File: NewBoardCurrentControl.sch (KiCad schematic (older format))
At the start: 19 parts, among them Q1 RSR030N06TL, U6 ADA4528-2ACPZ-RL, U7 782853152_WE-CBA_08

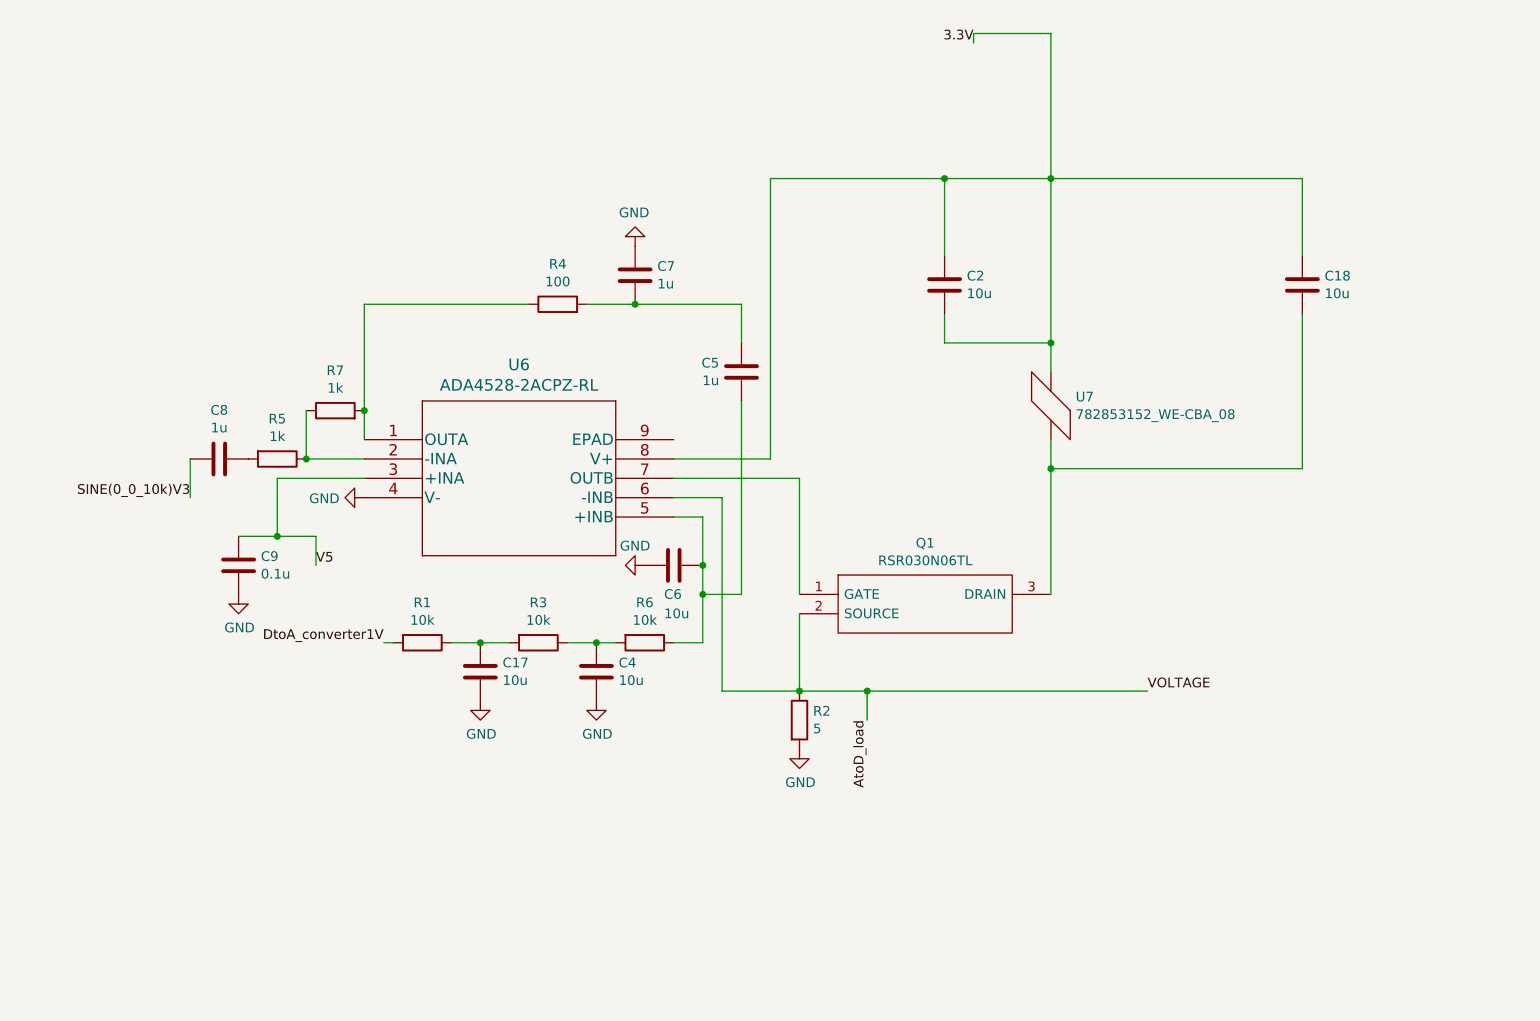
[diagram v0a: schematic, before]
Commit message: QA'd, added 2 caps, noted where laser should be
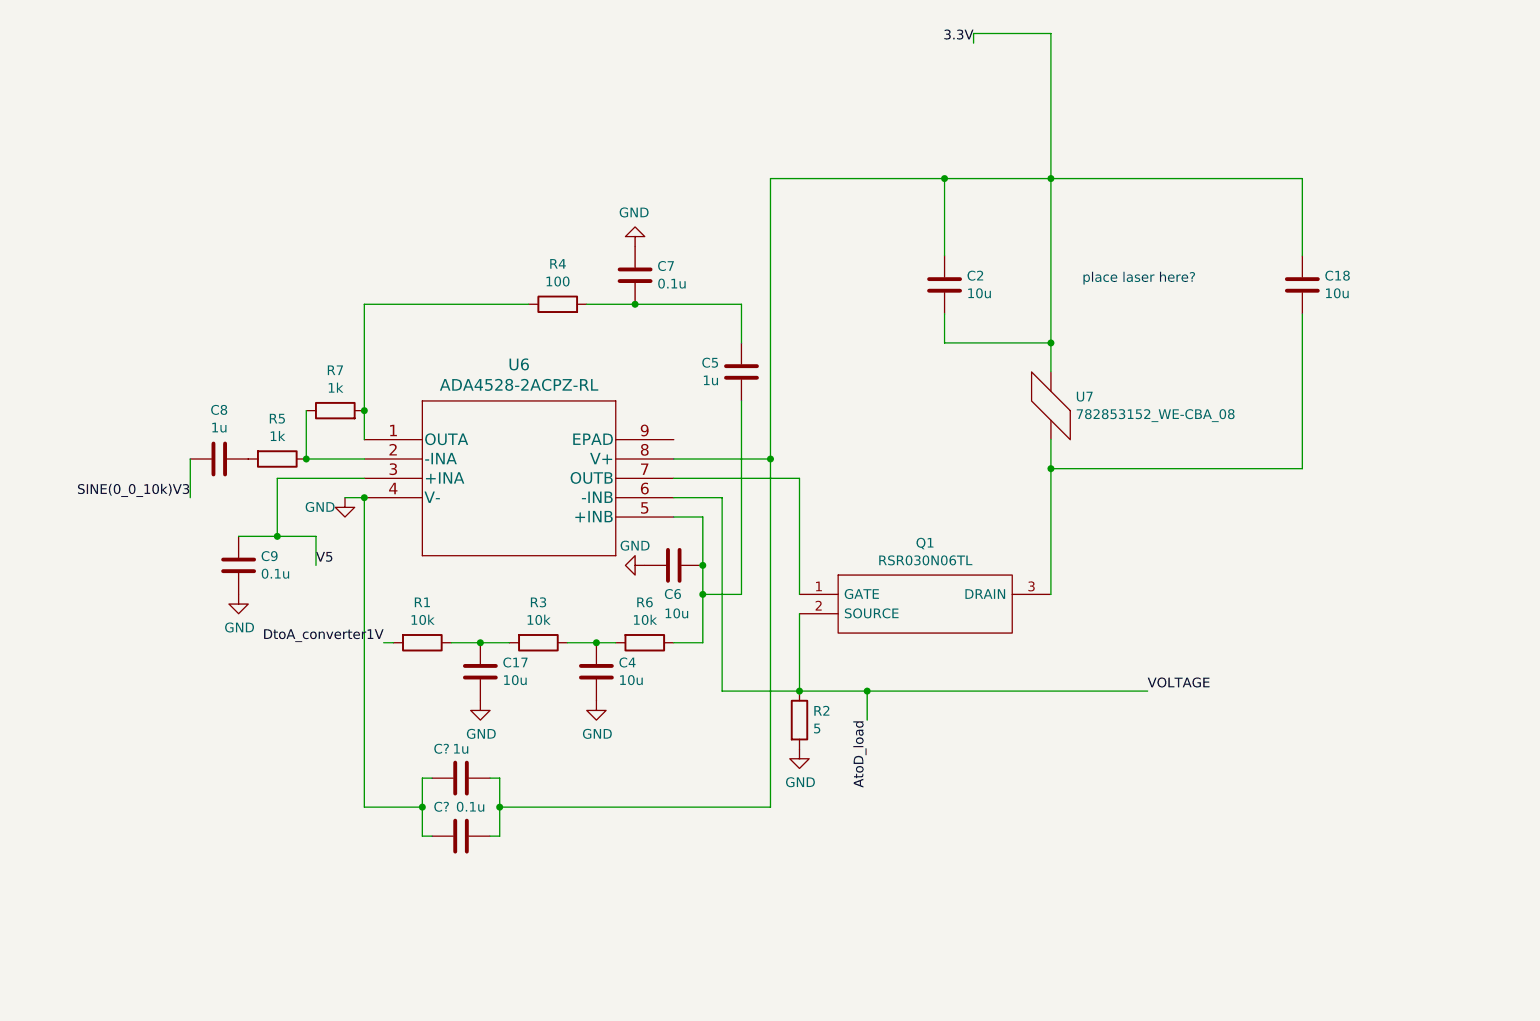
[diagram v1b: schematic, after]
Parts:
- added C?: 1u, symbol Device:C
- added C?: 0.1u, symbol Device:C
- C7: value 1u -> 0.1u
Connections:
- net 3.3V: now also C?.1, C?.1
- net GND: now also C?.2, C?.2
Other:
- note added: "place laser here?\n"
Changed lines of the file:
@@
 L power:GND #PWR0102
 U 1 1 60C997A8
-P 4500 3850
-F 0 "#PWR0102" H 4500 3600 50  0001 C CNN
-F 1 "GND" V 4505 3722 50  0000 R CNN
-F 2 "" H 4500 3850 50  0001 C CNN
-F 3 "" H 4500 3850 50  0001 C CNN
-	1    4500 3850
-	0    1    1    0
+P 4400 3850
+F 0 "#PWR0102" H 4400 3600 50  0001 C CNN
+F 1 "GND" H 4350 3800 50  0000 R CNN
+F 2 "" H 4400 3850 50  0001 C CNN
+F 3 "" H 4400 3850 50  0001 C CNN
+	1    4400 3850
+	1    0    0    -1
 $EndComp
 $Comp
@@
 P 5900 2700
 F 0 "C7" H 6015 2746 50  0000 L CNN
-F 1 "1u" H 6015 2655 50  0000 L CNN
+F 1 "0.1u" H 6015 2655 50  0000 L CNN
 F 2 "" H 5938 2550 50  0001 C CNN
 F 3 "~" H 5900 2700 50  0001 C CNN
@@
 Wire Wire Line
 	8050 3550 8050 3700
+Wire Wire Line
+	4500 3850 4500 5450
+Wire Wire Line
+	4500 5450 4800 5450
+Wire Wire Line
+	4800 5450 4800 5300
+Wire Wire Line
+	4800 5300 4850 5300
+$Comp
+L Device:C C?
+U 1 1 60D13632
+P 5000 5300
+F 0 "C?" V 4850 5200 50  0000 C CNN
+F 1 "1u" V 4850 5300 50  0000 C CNN
+F 2 "" H 5038 5150 50  0001 C CNN
+F 3 "~" H 5000 5300 50  0001 C CNN
+	1    5000 5300
+	0    1    1    0
+$EndComp
+$Comp
+L Device:C C?
+U 1 1 60D13F2E
+P 5000 5600
+F 0 "C?" V 4850 5500 50  0000 C CNN
+F 1 "0.1u" V 4850 5650 50  0000 C CNN
+F 2 "" H 5038 5450 50  0001 C CNN
+F 3 "~" H 5000 5600 50  0001 C CNN
+	1    5000 5600
+	0    1    1    0
+$EndComp
+Wire Wire Line
+	4800 5450 4800 5600
+Wire Wire Line
+	4800 5600 4850 5600
+Connection ~ 4800 5450
+Wire Wire Line
+	5150 5600 5200 5600
+Wire Wire Line
+	5200 5600 5200 5450
+Wire Wire Line
+	5200 5450 6600 5450
+Wire Wire Line
+	6600 5450 6600 3650
+Connection ~ 6600 3650
+Wire Wire Line
+	5150 5300 5200 5300
+Wire Wire Line
+	5200 5300 5200 5450
+Connection ~ 5200 5450
+Wire Wire Line
+	4500 3850 4400 3850
+Connection ~ 4500 3850
+Text Notes 8800 2750 2    50   ~ 0
+place laser here?\n
 $EndSCHEMATC

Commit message: cache
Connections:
- net 3.3V renamed V2_3.3V
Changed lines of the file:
@@
 Wire Wire Line
 	8050 1450 7650 1450
-Wire Wire Line
-	7650 1450 7650 1500
 $Comp
 L Device:C C2
@@
 Text Label 4250 4200 0    50   ~ 0
 V5
-Text Label 7650 1500 2    50   ~ 0
-3.3V
 Connection ~ 8050 3050
 Connection ~ 8050 3700
@@
 Text Notes 8800 2750 2    50   ~ 0
 place laser here?\n
+Text Label 7650 1450 2    50   ~ 0
+V2_3.3V
 $EndSCHEMATC

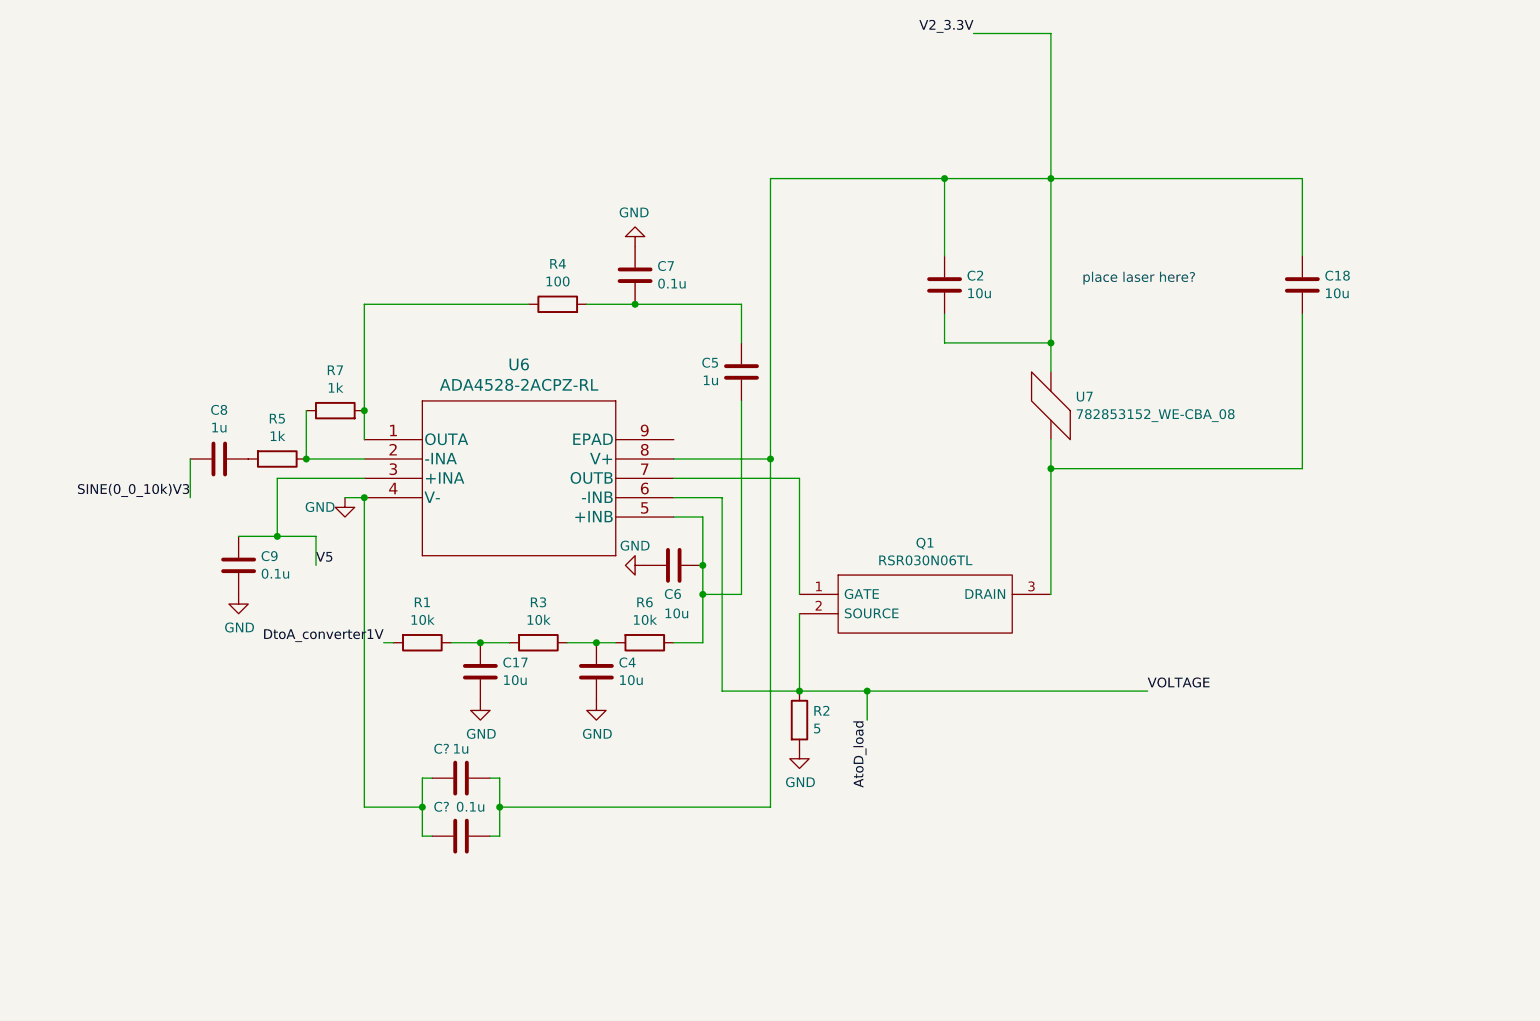
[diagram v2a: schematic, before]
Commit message: annotate all sheets
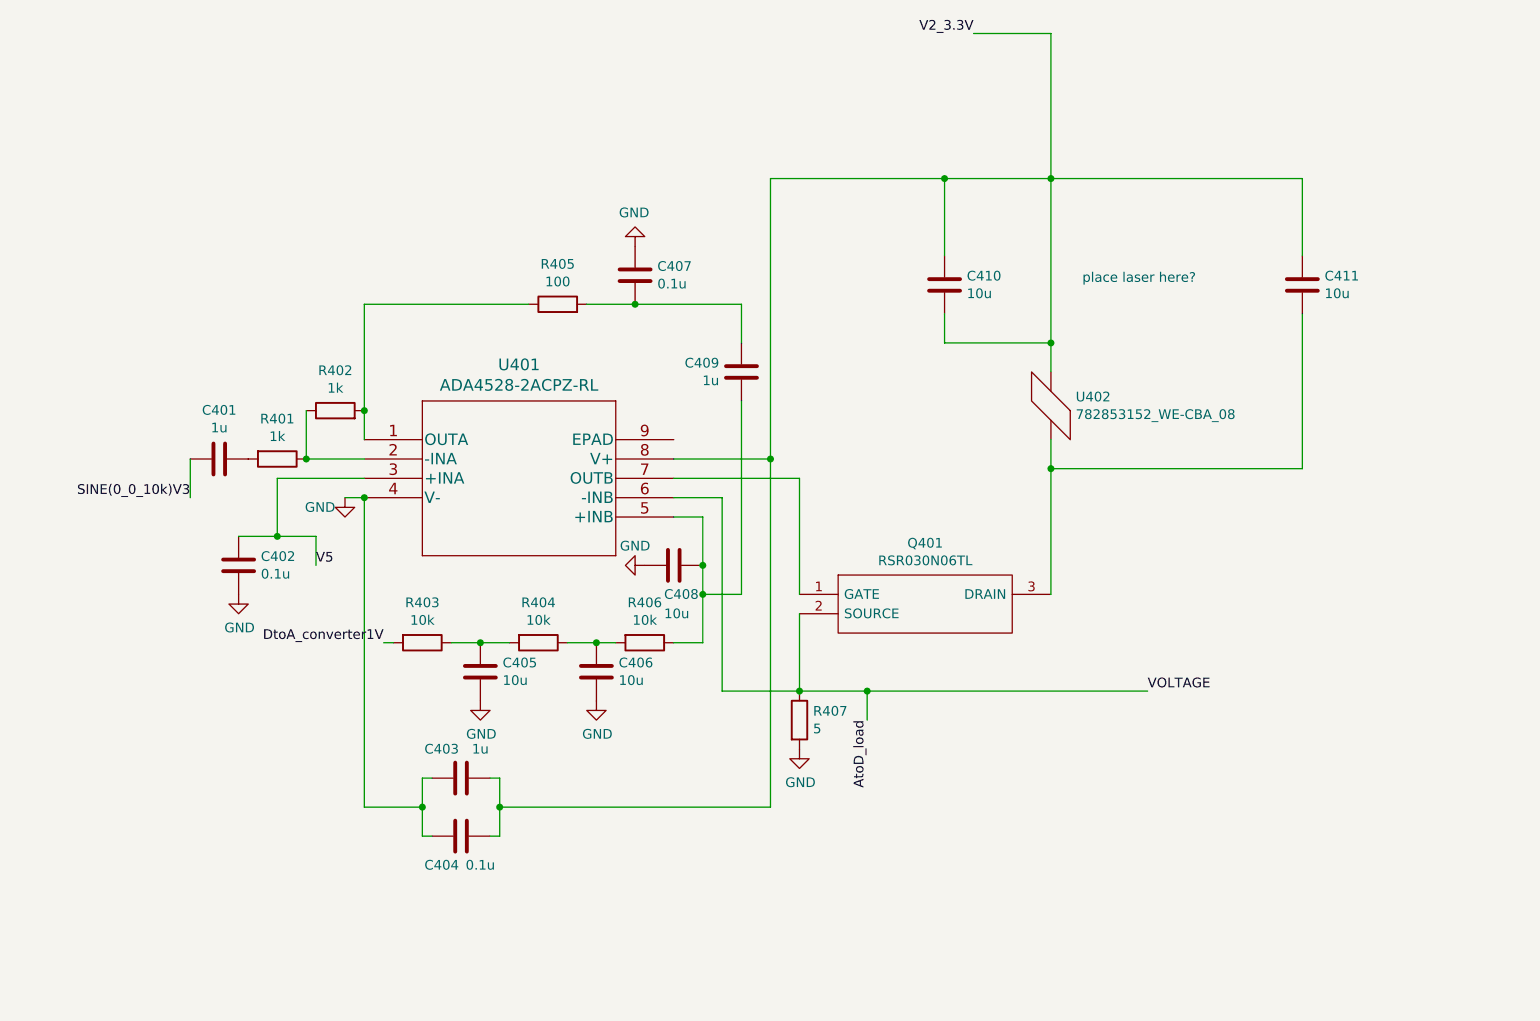
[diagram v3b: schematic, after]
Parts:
- gave numbers to parts that had none: 2
- renumbered C8 to C401, C9 to C402, C17 to C405, C4 to C406, C7 to C407, C6 to C408, C5 to C409, C2 to C410, C18 to C411, Q1 to Q401, R5 to R401, R7 to R402, R1 to R403, R3 to R404, R4 to R405, R6 to R406, R2 to R407, U6 to U401, U7 to U402
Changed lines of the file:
@@
 $EndDescr
 $Comp
-L ADA4528-2ACPZ-RL:ADA4528-2ACPZ-RL U6
+L ADA4528-2ACPZ-RL:ADA4528-2ACPZ-RL U401
 U 1 1 60C850F4
 P 4500 3550
-F 0 "U6" H 5300 3937 60  0000 C CNN
+F 0 "U401" H 5300 3937 60  0000 C CNN
 F 1 "ADA4528-2ACPZ-RL" H 5300 3831 60  0000 C CNN
 F 2 "CP_8_11_ADI" H 5300 3790 60  0001 C CNN
@@
 $EndComp
 $Comp
-L RSR030N06TL:RSR030N06TL Q1
+L RSR030N06TL:RSR030N06TL Q401
 U 1 1 60C86B21
 P 6750 4350
-F 0 "Q1" H 7400 4615 50  0000 C CNN
+F 0 "Q401" H 7400 4615 50  0000 C CNN
 F 1 "RSR030N06TL" H 7400 4524 50  0000 C CNN
 F 2 "SOT95P280X100-3N" H 7900 4450 50  0001 L CNN
@@
 	8050 1450 7650 1450
 $Comp
-L Device:C C2
+L Device:C C410
 U 1 1 60C8E619
 P 7500 2750
-F 0 "C2" H 7615 2796 50  0000 L CNN
+F 0 "C410" H 7615 2796 50  0000 L CNN
 F 1 "10u" H 7615 2705 50  0000 L CNN
 F 2 "" H 7538 2600 50  0001 C CNN
@@
 $EndComp
 $Comp
-L Device:C C18
+L Device:C C411
 U 1 1 60C8ED48
 P 9350 2750
-F 0 "C18" H 9465 2796 50  0000 L CNN
+F 0 "C411" H 9465 2796 50  0000 L CNN
 F 1 "10u" H 9465 2705 50  0000 L CNN
 F 2 "" H 9388 2600 50  0001 C CNN
@@
 Connection ~ 6750 4850
 $Comp
-L Device:R R2
+L Device:R R407
 U 1 1 60C96966
 P 6750 5000
-F 0 "R2" H 6820 5046 50  0000 L CNN
+F 0 "R407" H 6820 5046 50  0000 L CNN
 F 1 "5" H 6820 4955 50  0000 L CNN
 F 2 "" V 6680 5000 50  0001 C CNN
@@
 $EndComp
 $Comp
-L power:GND #PWR0101
+L power:GND #PWR0407
 U 1 1 60C97896
 P 6750 5150
-F 0 "#PWR0101" H 6750 4900 50  0001 C CNN
+F 0 "#PWR0407" H 6750 4900 50  0001 C CNN
 F 1 "GND" H 6755 4977 50  0000 C CNN
 F 2 "" H 6750 5150 50  0001 C CNN
@@
 	7100 4850 8550 4850
 $Comp
-L power:GND #PWR0102
+L power:GND #PWR0402
 U 1 1 60C997A8
 P 4400 3850
-F 0 "#PWR0102" H 4400 3600 50  0001 C CNN
+F 0 "#PWR0402" H 4400 3600 50  0001 C CNN
 F 1 "GND" H 4350 3800 50  0000 R CNN
 F 2 "" H 4400 3850 50  0001 C CNN
@@
 $EndComp
 $Comp
-L Device:R R6
+L Device:R R406
 U 1 1 60C9BFE0
 P 5950 4600
-F 0 "R6" V 5743 4600 50  0000 C CNN
+F 0 "R406" V 5743 4600 50  0000 C CNN
 F 1 "10k" V 5834 4600 50  0000 C CNN
 F 2 "" V 5880 4600 50  0001 C CNN
@@
 	5800 4600 5700 4600
 $Comp
-L Device:C C4
+L Device:C C406
 U 1 1 60C9CF21
 P 5700 4750
-F 0 "C4" H 5815 4796 50  0000 L CNN
+F 0 "C406" H 5815 4796 50  0000 L CNN
 F 1 "10u" H 5815 4705 50  0000 L CNN
 F 2 "" H 5738 4600 50  0001 C CNN
@@
 Connection ~ 5700 4600
 $Comp
-L power:GND #PWR0103
+L power:GND #PWR0404
 U 1 1 60C9DA38
 P 5700 4900
-F 0 "#PWR0103" H 5700 4650 50  0001 C CNN
+F 0 "#PWR0404" H 5700 4650 50  0001 C CNN
 F 1 "GND" H 5705 4727 50  0000 C CNN
 F 2 "" H 5700 4900 50  0001 C CNN
@@
 	5700 4600 5550 4600
 $Comp
-L Device:R R3
+L Device:R R404
 U 1 1 60C9E5A0
 P 5400 4600
-F 0 "R3" V 5193 4600 50  0000 C CNN
+F 0 "R404" V 5193 4600 50  0000 C CNN
 F 1 "10k" V 5284 4600 50  0000 C CNN
 F 2 "" V 5330 4600 50  0001 C CNN
@@
 $EndComp
 $Comp
-L Device:C C17
+L Device:C C405
 U 1 1 60C9EA80
 P 5100 4750
-F 0 "C17" H 5215 4796 50  0000 L CNN
+F 0 "C405" H 5215 4796 50  0000 L CNN
 F 1 "10u" H 5215 4705 50  0000 L CNN
 F 2 "" H 5138 4600 50  0001 C CNN
@@
 $EndComp
 $Comp
-L power:GND #PWR0104
+L power:GND #PWR0403
 U 1 1 60C9F219
 P 5100 4900
-F 0 "#PWR0104" H 5100 4650 50  0001 C CNN
+F 0 "#PWR0403" H 5100 4650 50  0001 C CNN
 F 1 "GND" H 5105 4727 50  0000 C CNN
 F 2 "" H 5100 4900 50  0001 C CNN
@@
 	5100 4600 5250 4600
 $Comp
-L Device:R R1
+L Device:R R403
 U 1 1 60CA0508
 P 4800 4600
-F 0 "R1" V 4593 4600 50  0000 C CNN
+F 0 "R403" V 4593 4600 50  0000 C CNN
 F 1 "10k" V 4684 4600 50  0000 C CNN
 F 2 "" V 4730 4600 50  0001 C CNN
@@
 	6250 4600 6100 4600
 $Comp
-L Device:C C6
+L Device:C C408
 U 1 1 60CA1AED
 P 6100 4200
-F 0 "C6" V 6250 4150 50  0000 L CNN
+F 0 "C408" V 6250 4150 50  0000 L CNN
 F 1 "10u" V 6350 4150 50  0000 L CNN
 F 2 "" H 6138 4050 50  0001 C CNN
@@
 $EndComp
 $Comp
-L power:GND #PWR0105
+L power:GND #PWR0406
 U 1 1 60CA2096
 P 5950 4200
-F 0 "#PWR0105" H 5950 3950 50  0001 C CNN
+F 0 "#PWR0406" H 5950 3950 50  0001 C CNN
 F 1 "GND" V 5850 4150 50  0000 C CNN
 F 2 "" H 5950 4200 50  0001 C CNN
@@
 Connection ~ 7500 2200
 $Comp
-L Device:R R5
+L Device:R R401
 U 1 1 60CA58D6
 P 4050 3650
-F 0 "R5" V 3843 3650 50  0000 C CNN
+F 0 "R401" V 3843 3650 50  0000 C CNN
 F 1 "1k" V 3934 3650 50  0000 C CNN
 F 2 "" V 3980 3650 50  0001 C CNN
@@
 $EndComp
 $Comp
-L Device:C C8
+L Device:C C401
 U 1 1 60CA66EF
 P 3750 3650
-F 0 "C8" V 3498 3650 50  0000 C CNN
+F 0 "C401" V 3498 3650 50  0000 C CNN
 F 1 "1u" V 3589 3650 50  0000 C CNN
 F 2 "" H 3788 3500 50  0001 C CNN
@@
 	3600 3650 3600 3850
 $Comp
-L Device:R R7
+L Device:R R402
 U 1 1 60CA8746
 P 4350 3400
-F 0 "R7" V 4557 3400 50  0000 C CNN
+F 0 "R402" V 4557 3400 50  0000 C CNN
 F 1 "1k" V 4466 3400 50  0000 C CNN
 F 2 "" V 4280 3400 50  0001 C CNN
@@
 Connection ~ 4200 3650
 $Comp
-L Device:C C7
+L Device:C C407
 U 1 1 60CB00E4
 P 5900 2700
-F 0 "C7" H 6015 2746 50  0000 L CNN
+F 0 "C407" H 6015 2746 50  0000 L CNN
 F 1 "0.1u" H 6015 2655 50  0000 L CNN
 F 2 "" H 5938 2550 50  0001 C CNN
@@
 $EndComp
 $Comp
-L power:GND #PWR0106
+L power:GND #PWR0405
 U 1 1 60CB0BD8
 P 5900 2550
-F 0 "#PWR0106" H 5900 2300 50  0001 C CNN
+F 0 "#PWR0405" H 5900 2300 50  0001 C CNN
 F 1 "GND" H 5905 2377 50  0000 C CNN
 F 2 "" H 5900 2550 50  0001 C CNN
@@
 	5900 2850 5650 2850
 $Comp
-L Device:R R4
+L Device:R R405
 U 1 1 60CB730A
 P 5500 2850
-F 0 "R4" V 5707 2850 50  0000 C CNN
+F 0 "R405" V 5707 2850 50  0000 C CNN
 F 1 "100" V 5616 2850 50  0000 C CNN
 F 2 "" V 5430 2850 50  0001 C CNN
@@
 	6600 2200 6600 3650
 $Comp
-L Device:C C5
+L Device:C C409
 U 1 1 60CA302B
 P 6450 3200
-F 0 "C5" H 6565 3246 50  0000 L CNN
+F 0 "C409" H 6565 3246 50  0000 L CNN
 F 1 "1u" H 6565 3155 50  0000 L CNN
 F 2 "" H 6488 3050 50  0001 C CNN
@@
 	4050 4050 3850 4050
 $Comp
-L Device:C C9
+L Device:C C402
 U 1 1 60CD4C5B
 P 3850 4200
-F 0 "C9" H 3735 4154 50  0000 R CNN
+F 0 "C402" H 3735 4154 50  0000 R CNN
 F 1 "0.1u" H 3735 4245 50  0000 R CNN
 F 2 "" H 3888 4050 50  0001 C CNN
@@
 $EndComp
 $Comp
-L power:GND #PWR0107
+L power:GND #PWR0401
 U 1 1 60CD6A5A
 P 3850 4350
-F 0 "#PWR0107" H 3850 4100 50  0001 C CNN
+F 0 "#PWR0401" H 3850 4100 50  0001 C CNN
 F 1 "GND" H 3855 4177 50  0000 C CNN
 F 2 "" H 3850 4350 50  0001 C CNN
@@
 Connection ~ 8050 3700
 $Comp
-L New_Library_for_first_symbol:782853152_WE-CBA_08 U7
+L New_Library_for_first_symbol:782853152_WE-CBA_08 U402
 U 1 1 60D001D1
 P 8050 3400
-F 0 "U7" V 7979 3528 50  0000 L CNN
+F 0 "U402" V 7979 3528 50  0000 L CNN
 F 1 "782853152_WE-CBA_08" V 8070 3528 50  0000 L CNN
 F 2 "" H 8150 3400 50  0001 C CNN
@@
 	4800 5300 4850 5300
 $Comp
-L Device:C C?
+L Device:C C403
 U 1 1 60D13632
 P 5000 5300
-F 0 "C?" V 4850 5200 50  0000 C CNN
-F 1 "1u" V 4850 5300 50  0000 C CNN
+F 0 "C403" V 4850 5200 50  0000 C CNN
+F 1 "1u" V 4850 5400 50  0000 C CNN
 F 2 "" H 5038 5150 50  0001 C CNN
 F 3 "~" H 5000 5300 50  0001 C CNN
@@
 $EndComp
 $Comp
-L Device:C C?
+L Device:C C404
 U 1 1 60D13F2E
 P 5000 5600
-F 0 "C?" V 4850 5500 50  0000 C CNN
-F 1 "0.1u" V 4850 5650 50  0000 C CNN
+F 0 "C404" V 5150 5500 50  0000 C CNN
+F 1 "0.1u" V 5150 5700 50  0000 C CNN
 F 2 "" H 5038 5450 50  0001 C CNN
 F 3 "~" H 5000 5600 50  0001 C CNN
